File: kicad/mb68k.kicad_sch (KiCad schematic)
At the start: 0 parts

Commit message: Arduino and kicad work
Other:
- added sheet DUART (DUART.kicad_sch)
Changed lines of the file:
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@@
+    )
+  )
+  (sheet (at 121.92 64.77) (size 13.97 16.51) (fields_autoplaced)
+    (stroke (width 0.1524) (type solid) (color 0 0 0 0))
+    (fill (color 0 0 0 0.0000))
+    (property "Sheet name" "DUART" (id 0) (at 121.92 64.0584 0)
+      (effects (font (size 1.27 1.27)) (justify left bottom))
+    )
+    (property "Sheet file" "DUART.kicad_sch" (id 1) (at 121.92 81.8646 0)
+      (effects (font (size 1.27 1.27)) (justify left top))
     )
   )
@@
     (path "/60b3e0cc-7d6f-4628-b20d-5a9d7b2fa5fa" (page "2"))
     (path "/c0b233c3-0354-40a8-9da4-8134543aeba9" (page "3"))
+    (path "/c382627c-aaa0-47a5-a0f7-b0da34ce6bae" (page "4"))
   )
   (symbol_instances
@@
       (reference "U?") (unit 1) (value "68010P10") (footprint "")
     )
+    (path "/c382627c-aaa0-47a5-a0f7-b0da34ce6bae/5a8daa73-8d7c-4391-b18d-0c250a2bb8bf"
+      (reference "U?") (unit 1) (value "68681") (footprint "")
+    )
     (path "/c0b233c3-0354-40a8-9da4-8134543aeba9/62e3e07a-9380-4c51-acc0-e502eba8f249"

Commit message: cleanup
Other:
- added sheet DTACK and IRQ circuit (dtack_irq.kicad_sch)

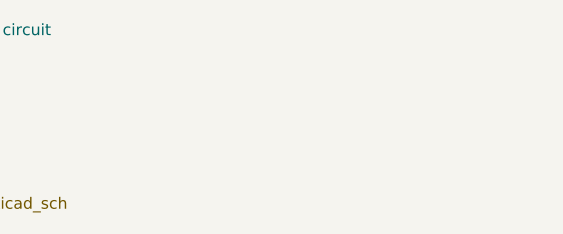
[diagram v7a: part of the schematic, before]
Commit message: - Added buffers for LED indicators in kicad - Removed pullups on FC0.2 in kicad - Connected FC0-2 to glue logic in kicad - Revamped glue logic for irg and iack in Digital
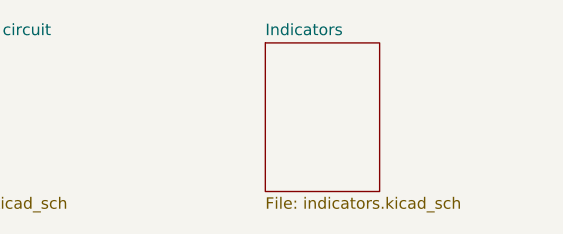
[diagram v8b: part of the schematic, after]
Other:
- added sheet Indicators (indicators.kicad_sch)
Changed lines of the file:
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@@
     (rev "1.0-bboard")
+  )
+  (sheet (at 195.58 64.77) (size 12.7 16.51) (fields_autoplaced)
+    (stroke (width 0.1524) (type solid))
+    (fill (color 0 0 0 0.0000))
+    (property "Sheetname" "Indicators" (at 195.58 64.0584 0)
+      (effects (font (size 1.27 1.27)) (justify left bottom))
+    )
+    (property "Sheetfile" "indicators.kicad_sch" (at 195.58 81.8646 0)
+      (effects (font (size 1.27 1.27)) (justify left top))
+    )
+    (instances
+      (project "mb68k"
+        (path "/e63e39d7-6ac0-4ffd-8aa3-1841a4541b55" (page "6"))
+      )
+    )
   )
   (sheet (at 58.42 64.77) (size 11.43 16.51) (fields_autoplaced)
